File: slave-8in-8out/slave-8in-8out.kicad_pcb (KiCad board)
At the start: 2 copper layers, 61 x 72.4 mm, 87 parts, among them J1 Conn_01x06_Male, J2 Screw_Terminal_01x02, J3 Conn_01x06_Female, J4 Screw_Terminal_01x04, J5 Screw_Terminal_01x04, J6 Screw_Terminal_01x04, J7 Screw_Terminal_01x04, J8 Conn_01x10_Male, J9 Screw_Terminal_01x02, SW1 SW_DIP_x05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

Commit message: update slave-8in-8out pcb
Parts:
- moved R1 7.47 mm to (70.6, 96.5), turned to 0 degrees
- moved R2 5.71 mm to (70.6, 97.8), turned to 0 degrees
- moved D3 1.27 mm to (105.9, 104.6)
- moved D7 1.27 mm to (93.2, 104.6)
- moved R47 1.27 mm to (111.3, 106.9)
- moved R53 1.27 mm to (95.8, 106.9)
- moved R54 1.27 mm to (100.8, 106.9)
- moved D1 1.27 mm to (111.2, 104.6)
- moved D2 1.27 mm to (108.5, 104.6)
- moved D4 1.27 mm to (103.4, 104.6)
- moved D5 1.27 mm to (100.8, 104.6)
- moved D6 1.27 mm to (98.3, 104.6)
- moved D8 1.27 mm to (95.8, 104.6)
- moved J8 1.27 mm to (90.7, 111.3)
- moved R48 1.27 mm to (108.5, 106.9)
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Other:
- board text removed: "SCL"

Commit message: slave-8in-8out-0.1
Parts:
- removed R11: 10k, Resistor_SMD:R_0402_1005Metric
- U1: value MCP23017_SO -> PCF8575; footprint Package_SO:SOIC-28W_7.5x17.9mm_P1.27mm -> Package_SO:SSOP-24_5.3x8.2mm_P0.65mm
- moved H2 83.9 mm to (135.6, 63.8)
- moved H4 60.1 mm to (135.6, 128.3)
- moved H3 51.0 mm to (73.2, 128.3)
- moved J3 14.9 mm to (128.2, 101.3)
- moved U10 14.1 mm to (115.3, 96.7)
- moved U1 12.0 mm to (95.0, 96.7), turned to 0 degrees
- moved D1 11.6 mm to (122.2, 108.7)
- moved D3 11.6 mm to (116.8, 108.7)
- moved D5 11.6 mm to (111.8, 108.7)
- moved D7 11.6 mm to (104.1, 108.7)
- moved D8 11.6 mm to (106.7, 108.7)
- moved J8 11.6 mm to (101.6, 115.3)
- moved R47 11.6 mm to (122.2, 111.0)
- moved R48 11.6 mm to (119.4, 111.0)
- moved R50 11.6 mm to (114.3, 111.0)
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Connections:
- D7 pad 2: GPB7 -> GPA1
- D8 pad 2: GPA1 -> GPA0
- R46 pad 1: GPA0 -> GPB7
- U1 pad 1: GPB0 -> unconnected-(U1-Pad1)
- U1 pad 10: GND -> GPB6
- U1 pad 11: unconnected-(U1-Pad11) -> GPB7
- U1 pad 12: SCL -> GND
- U1 pad 13: SDA -> GPA0
- U1 pad 14: unconnected-(U1-Pad14) -> GPA1
- U1 pad 15: A0 -> GPA2
- U1 pad 16: A1 -> GPA3
- U1 pad 17: A2 -> GPA4
- U1 pad 18: Net-(R11-Pad1) -> GPA5
- U1 pad 19: unconnected-(U1-Pad19) -> GPA6
- U1 pad 2: GPB1 -> A1
- U1 pad 20: unconnected-(U1-Pad20) -> GPA7
- U1 pad 21: GPA0 -> A0
- U1 pad 22: GPA1 -> SCL
- U1 pad 23: GPA2 -> SDA
- U1 pad 24: GPA3 -> +3V3
- U1 pad 3: GPB2 -> A2
- U1 pad 4: GPB3 -> GPB0
- U1 pad 5: GPB4 -> GPB1
- U1 pad 6: GPB5 -> GPB2
- U1 pad 7: GPB6 -> GPB3
- U1 pad 8: GPB7 -> GPB4
- U1 pad 9: +3V3 -> GPB5
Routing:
- net +5V: track 0.00 -> 179.3 mm
- net GNDPWR: track 0.00 -> 169.6 mm
- net LED_GNDPWR: track 0.00 -> 156.4 mm, vias 0 -> 4
- net GND: track 0.00 -> 136.3 mm, vias 0 -> 5
- net +3V3: track 0.00 -> 92.1 mm, vias 0 -> 3
- net SCL: track 0.00 -> 77.7 mm, vias 0 -> 2
- net SDA: track 0.00 -> 67.6 mm, vias 0 -> 7
- net GPA4: track 0.00 -> 50.0 mm
- net A2: track 0.00 -> 48.5 mm, vias 0 -> 2
- net LED_GND: track 0.00 -> 47.8 mm
- net GPA6: track 0.00 -> 47.7 mm, vias 0 -> 3
- net A1: track 0.00 -> 46.8 mm, vias 0 -> 2
- net GPA7: track 0.00 -> 44.2 mm, vias 0 -> 3
- net GPB7: track 0.00 -> 43.1 mm, vias 0 -> 2
- net GPA5: track 0.00 -> 43.1 mm, vias 0 -> 3
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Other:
- board size 61 x 72.4 mm -> 69.6 x 71.6 mm
- board text added: "3.3V"
- board text added: "5V"
- board text added: "GNDPWR"
- board text added: "SCL"
- board text added: "SDA"
- board text added: "slave-8in-8out-0.1"
- board text removed: "1-2-3 Address"
- board text removed: "4-5 Led"
- board text removed: "brick slave 8in/8out v1.1"

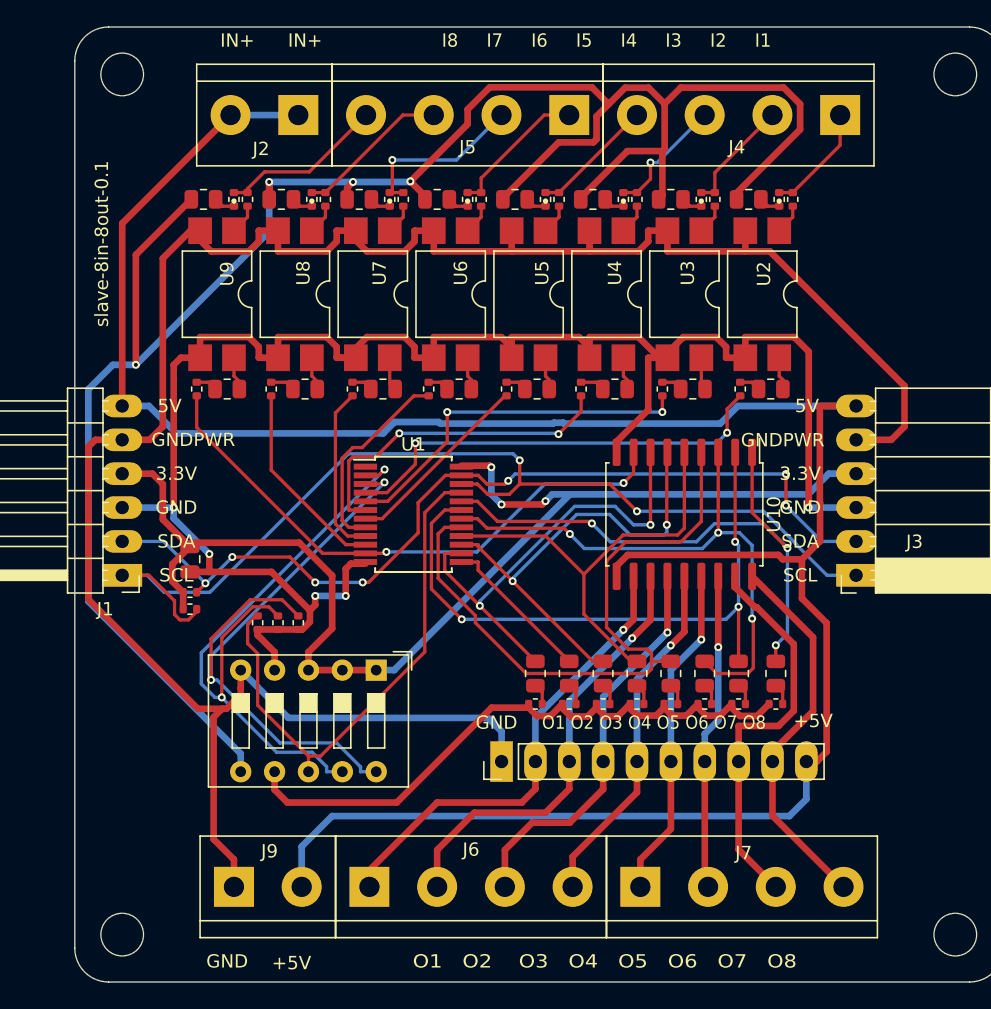
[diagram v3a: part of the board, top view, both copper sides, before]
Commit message: refactoring slave-8in-8out
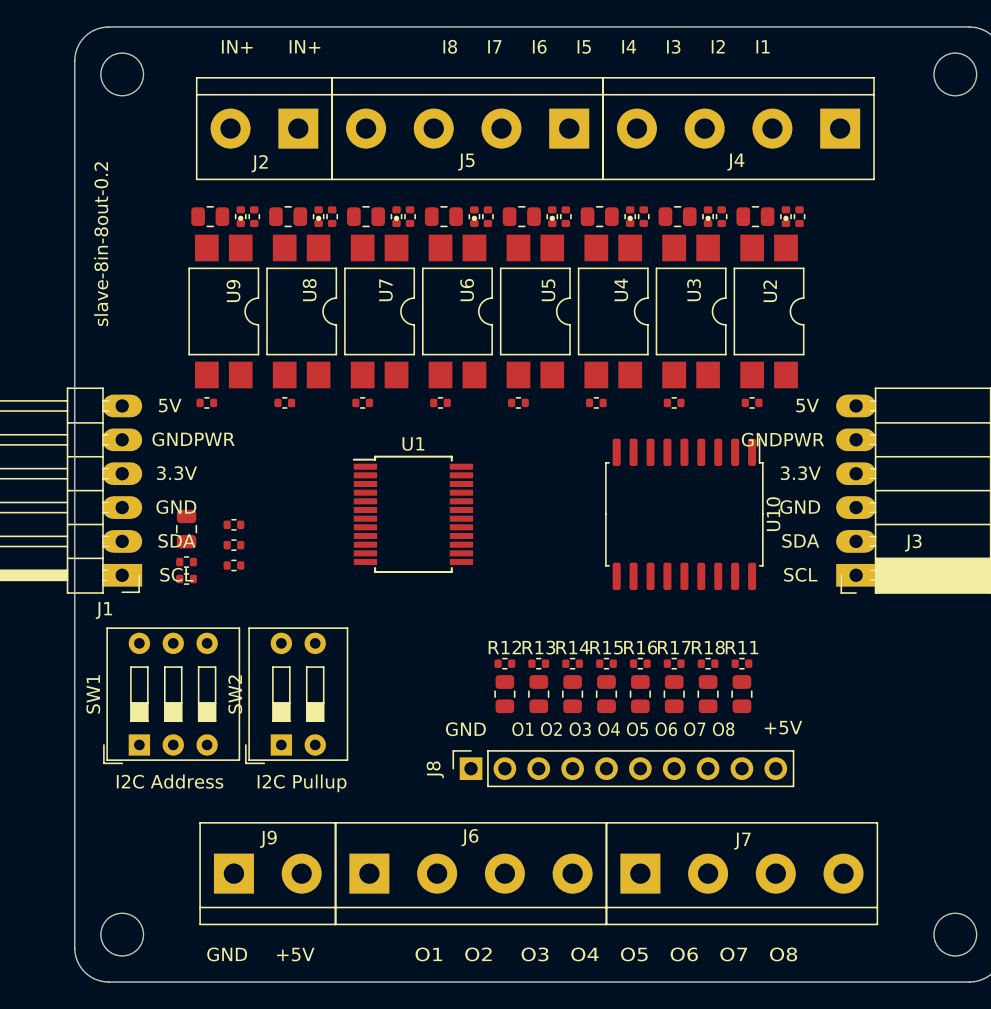
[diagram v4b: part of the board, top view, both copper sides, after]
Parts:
- removed D10, D12, D14, D16, D18, D20, D22, D24: LED, Resistor_SMD:R_0805_2012Metric
- removed R47, R48, R49, R50, R51, R52, R53, R54: 330, Resistor_SMD:R_0402_1005Metric
- added R11: 680, Resistor_SMD:R_0402_1005Metric, F.Cu at (119.6, 108.0)
- added R12: 680, Resistor_SMD:R_0402_1005Metric, F.Cu at (101.9, 108.0)
- added R13: 680, Resistor_SMD:R_0402_1005Metric, F.Cu at (104.4, 108.0)
- added R14: 680, Resistor_SMD:R_0402_1005Metric, F.Cu at (106.9, 108.0)
- added R15: 680, Resistor_SMD:R_0402_1005Metric, F.Cu at (109.5, 108.0)
- added R16: 680, Resistor_SMD:R_0402_1005Metric, F.Cu at (112.0, 108.0)
- added R17: 680, Resistor_SMD:R_0402_1005Metric, F.Cu at (114.6, 108.0)
- added R18: 680, Resistor_SMD:R_0402_1005Metric, F.Cu at (117.1, 108.0)
- added SW2: SW_DIP_x02, Button_Switch_THT:SW_DIP_SPSTx02_Slide_9.78x7.26mm_W7.62mm_P2.54mm, F.Cu at (85.1, 114.0)
- J8: value Conn_01x10_Male -> Conn_01x10_Female; footprint Connector_PinHeader_2.54mm:PinHeader_1x10_P2.54mm_Vertical -> Connector_PinSocket_2.54mm:PinSocket_1x10_P2.54mm_Vertical
- R31, R34, R37, R40, R43, R46, R5, R8: value 330 -> 10k
- SW1: value SW_DIP_x05 -> SW_DIP_x03; footprint Button_Switch_THT:SW_DIP_SPSTx05_Slide_9.78x14.88mm_W7.62mm_P2.54mm -> Button_Switch_THT:SW_DIP_SPSTx03_Slide_9.78x9.8mm_W7.62mm_P2.54mm
- moved D1 20.4 mm to (101.9, 110.2), turned to -90 degrees
- moved SW1 18.6 mm to (74.4, 114.0), turned to 90 degrees
- moved D2 15.1 mm to (104.4, 110.2), turned to -90 degrees
- moved D7 13.0 mm to (117.1, 110.2), turned to -90 degrees
- moved D8 13.0 mm to (119.6, 110.2), turned to -90 degrees
- moved D3 10.0 mm to (106.9, 110.2), turned to -90 degrees
- moved R28 8.79 mm to (81.5, 97.5), turned to 0 degrees
- moved R29 6.69 mm to (81.5, 99.1), turned to 0 degrees
- moved D6 5.55 mm to (114.6, 110.2), turned to -90 degrees
- moved D4 5.07 mm to (109.5, 110.2), turned to -90 degrees
- moved R30 4.65 mm to (81.5, 100.6), turned to 0 degrees
- moved J8 2.35 mm to (99.3, 115.8)
- moved C1 2.28 mm to (78.0, 97.9)
- moved R2 2.28 mm to (78.0, 101.6)
- moved R1 2.28 mm to (78.0, 100.3)
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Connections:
- C1 pad 2: GND -> LED_GND
- D1 pad 2: GPA7 -> O1
- D11 pad 1: LED_GNDPWR -> GNDPWR
- D13 pad 1: LED_GNDPWR -> GNDPWR
- D15 pad 1: LED_GNDPWR -> GNDPWR
- D17 pad 1: LED_GNDPWR -> GNDPWR
- D19 pad 1: LED_GNDPWR -> GNDPWR
- D2 pad 2: GPA6 -> O2
- D21 pad 1: LED_GNDPWR -> GNDPWR
- D23 pad 1: LED_GNDPWR -> GNDPWR
- D3 pad 2: GPA5 -> O3
- D4 pad 2: GPA4 -> O4
- D5 pad 2: GPA3 -> O5
- D6 pad 2: GPA2 -> O6
- D7 pad 2: GPA1 -> O7
- D8 pad 2: GPA0 -> O8
- D9 pad 1: LED_GNDPWR -> GNDPWR
- J1 pad 3: GND -> LED_GND
- J3 pad 3: GND -> LED_GND
- R1 pad 1: +3V3 -> Net-(R1-Pad1)
- R2 pad 1: +3V3 -> Net-(R2-Pad1)
- R28 pad 2: GND -> LED_GND
- R29 pad 2: GND -> LED_GND
- R30 pad 2: GND -> LED_GND
- R31 pad 1: GPB2 -> LED_GND
- R31 pad 2: Net-(D14-Pad2) -> GPB2
- R34 pad 1: GPB3 -> LED_GND
- R34 pad 2: Net-(D16-Pad2) -> GPB3
- R37 pad 1: GPB4 -> LED_GND
- R37 pad 2: Net-(D18-Pad2) -> GPB4
- R40 pad 1: GPB5 -> LED_GND
- R40 pad 2: Net-(D20-Pad2) -> GPB5
- R43 pad 1: GPB6 -> LED_GND
- R43 pad 2: Net-(D22-Pad2) -> GPB6
- R46 pad 1: GPB7 -> LED_GND
- R46 pad 2: Net-(D24-Pad2) -> GPB7
- R5 pad 1: GPB0 -> LED_GND
- R5 pad 2: Net-(D10-Pad2) -> GPB0
- R8 pad 1: GPB1 -> LED_GND
- R8 pad 2: Net-(D12-Pad2) -> GPB1
- SW1 pad 4: GND -> A0
- SW1 pad 5: GNDPWR -> A1
- SW1 pad 6: LED_GNDPWR -> A2
- U1 pad 12: GND -> LED_GND
- U10 pad 8: GPB7 -> GPA0
- U10 pad 9: GND -> LED_GND
- U2 pad 3: GND -> GPB0
- U2 pad 4: Net-(D10-Pad1) -> +3V3
- U3 pad 3: GND -> GPB1
- U3 pad 4: Net-(D12-Pad1) -> +3V3
- U4 pad 3: GND -> GPB2
- U4 pad 4: Net-(D14-Pad1) -> +3V3
- U5 pad 3: GND -> GPB3
- U5 pad 4: Net-(D16-Pad1) -> +3V3
- U6 pad 3: GND -> GPB4
- U6 pad 4: Net-(D18-Pad1) -> +3V3
- U7 pad 3: GND -> GPB5
- U7 pad 4: Net-(D20-Pad1) -> +3V3
- U8 pad 3: GND -> GPB6
- U8 pad 4: Net-(D22-Pad1) -> +3V3
- U9 pad 3: GND -> GPB7
- U9 pad 4: Net-(D24-Pad1) -> +3V3
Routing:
- net +5V: track 179.3 -> 0.00 mm
- net GNDPWR: track 169.6 -> 0.00 mm
- net LED_GNDPWR: track 156.4 -> 0.00 mm, vias 4 -> 0
- net GND: track 136.3 -> 0.00 mm, vias 5 -> 0
- net +3V3: track 92.1 -> 0.00 mm, vias 3 -> 0
- net SCL: track 77.7 -> 0.00 mm, vias 2 -> 0
- net SDA: track 67.6 -> 0.00 mm, vias 7 -> 0
- net GPA4: track 50.0 -> 0.00 mm
- net A2: track 48.5 -> 0.00 mm, vias 2 -> 0
- net LED_GND: track 47.8 -> 0.00 mm
- net GPA6: track 47.7 -> 0.00 mm, vias 3 -> 0
- net A1: track 46.8 -> 0.00 mm, vias 2 -> 0
- net GPA7: track 44.2 -> 0.00 mm, vias 3 -> 0
- net GPB7: track 43.1 -> 0.00 mm, vias 2 -> 0
- net GPA5: track 43.1 -> 0.00 mm, vias 3 -> 0
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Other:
- board text added: "I2C Address"
- board text added: "I2C Pullup"
- board text added: "slave-8in-8out-0.2"
- board text removed: "slave-8in-8out-0.1"

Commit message: update slave-8in-8out
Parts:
- added R19: 10k, Resistor_SMD:R_0402_1005Metric, F.Cu at (96.8, 93.0)
- added R20: 10k, Resistor_SMD:R_0402_1005Metric, F.Cu at (96.8, 94.5)
- added R21: 10k, Resistor_SMD:R_0402_1005Metric, F.Cu at (96.8, 97.5)
- added R22: 10k, Resistor_SMD:R_0402_1005Metric, F.Cu at (96.8, 96.0)
- added R23: 10k, Resistor_SMD:R_0402_1005Metric, F.Cu at (96.8, 99.1)
- added R24: 10k, Resistor_SMD:R_0402_1005Metric, F.Cu at (96.8, 100.6)
- added R25: 10k, Resistor_SMD:R_0402_1005Metric, F.Cu at (96.8, 102.1)
- added R26: 10k, Resistor_SMD:R_0402_1005Metric, F.Cu at (96.8, 103.6)
- moved U1 4.51 mm to (90.7, 98.0)
- moved D1 1.54 mm to (100.3, 110.5), turned to 90 degrees
- moved D2 1.54 mm to (102.9, 110.5), turned to 90 degrees
- moved D3 1.54 mm to (105.4, 110.5), turned to 90 degrees
- moved D4 1.54 mm to (108.0, 110.5), turned to 90 degrees
- moved D5 1.54 mm to (110.5, 110.5), turned to 90 degrees
- moved D6 1.54 mm to (113.0, 110.5), turned to 90 degrees
- moved D7 1.54 mm to (115.6, 110.5), turned to 90 degrees
- moved D8 1.54 mm to (118.1, 110.5), turned to 90 degrees
- moved R11 1.54 mm to (118.1, 108.2)
- moved R12 1.54 mm to (100.3, 108.2)
- moved R13 1.54 mm to (102.9, 108.2)
- moved R14 1.54 mm to (105.4, 108.2)
- moved R15 1.54 mm to (108.0, 108.2)
- moved R16 1.54 mm to (110.5, 108.2)
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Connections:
- C1 pad 2: LED_GND -> GND
- D1 pad 1: Net-(D1-Pad1) -> O0
- D1 pad 2: O1 -> Net-(R12-Pad1)
- D2 pad 1: Net-(D2-Pad1) -> O1
- D2 pad 2: O2 -> Net-(R13-Pad1)
- D3 pad 1: Net-(D3-Pad1) -> O2
- D3 pad 2: O3 -> Net-(R14-Pad1)
- D4 pad 1: Net-(D4-Pad1) -> O3
- D4 pad 2: O4 -> Net-(D4-Pad2)
- D5 pad 1: Net-(D5-Pad1) -> O4
- D5 pad 2: O5 -> Net-(D5-Pad2)
- D6 pad 1: Net-(D6-Pad1) -> O5
- D6 pad 2: O6 -> Net-(D6-Pad2)
- D7 pad 1: Net-(D7-Pad1) -> O6
- D7 pad 2: O7 -> Net-(D7-Pad2)
- D8 pad 1: Net-(D8-Pad1) -> O7
- D8 pad 2: O8 -> Net-(D8-Pad2)
- J1 pad 3: LED_GND -> GND
- J3 pad 3: LED_GND -> GND
- J4 pad 1: I1 -> I0
- J4 pad 2: I2 -> I1
- J4 pad 3: I3 -> I2
- J4 pad 4: I4 -> I3
- J5 pad 1: I5 -> I4
- J5 pad 2: I6 -> I5
- J5 pad 3: I7 -> I6
- J5 pad 4: I8 -> I7
- J6 pad 1: O1 -> O0
- J6 pad 2: O2 -> O1
- J6 pad 3: O3 -> O2
- J6 pad 4: O4 -> O3
- J7 pad 1: O5 -> O4
- J7 pad 2: O6 -> O5
- J7 pad 3: O7 -> O6
- J7 pad 4: O8 -> O7
- J8 pad 2: O1 -> O0
- J8 pad 3: O2 -> O1
- J8 pad 4: O3 -> O2
- J8 pad 5: O4 -> O3
- J8 pad 6: O5 -> O4
- J8 pad 7: O6 -> O5
- J8 pad 8: O7 -> O6
- J8 pad 9: O8 -> O7
- R10 pad 2: I3 -> I2
- R11 pad 1: Net-(D8-Pad1) -> Net-(D8-Pad2)
- R11 pad 2: LED_GND -> +5V
- R12 pad 1: Net-(D1-Pad1) -> Net-(R12-Pad1)
- R12 pad 2: LED_GND -> +5V
- R13 pad 1: Net-(D2-Pad1) -> Net-(R13-Pad1)
- R13 pad 2: LED_GND -> +5V
- R14 pad 1: Net-(D3-Pad1) -> Net-(R14-Pad1)
- R14 pad 2: LED_GND -> +5V
- R15 pad 1: Net-(D4-Pad1) -> Net-(D4-Pad2)
- R15 pad 2: LED_GND -> +5V
- R16 pad 1: Net-(D5-Pad1) -> Net-(D5-Pad2)
- R16 pad 2: LED_GND -> +5V
- R17 pad 1: Net-(D6-Pad1) -> Net-(D6-Pad2)
- R17 pad 2: LED_GND -> +5V
- R18 pad 1: Net-(D7-Pad1) -> Net-(D7-Pad2)
- R18 pad 2: LED_GND -> +5V
- R28 pad 2: LED_GND -> GND
- R29 pad 2: LED_GND -> GND
- R3 pad 1: I1 -> I0
- R30 pad 2: LED_GND -> GND
- R31 pad 1: LED_GND -> GND
- R32 pad 1: I4 -> I3
- R33 pad 2: I4 -> I3
- R34 pad 1: LED_GND -> GND
- R35 pad 1: I5 -> I4
- R36 pad 2: I5 -> I4
- R37 pad 1: LED_GND -> GND
- R38 pad 1: I6 -> I5
- R39 pad 2: I6 -> I5
- R4 pad 2: I1 -> I0
- R40 pad 1: LED_GND -> GND
- R41 pad 1: I7 -> I6
- R42 pad 2: I7 -> I6
- R43 pad 1: LED_GND -> GND
- R44 pad 1: I8 -> I7
- R45 pad 2: I8 -> I7
- R46 pad 1: LED_GND -> GND
- R5 pad 1: LED_GND -> GND
- R6 pad 1: I2 -> I1
- R7 pad 2: I2 -> I1
- R8 pad 1: LED_GND -> GND
- R9 pad 1: I3 -> I2
- U1 pad 12: LED_GND -> GND
- U10 pad 11: O1 -> O0
- U10 pad 12: O2 -> O1
- U10 pad 13: O3 -> O2
- U10 pad 14: O4 -> O3
- U10 pad 15: O5 -> O4
- U10 pad 16: O6 -> O5
- U10 pad 17: O7 -> O6
- U10 pad 18: O8 -> O7
- U10 pad 9: LED_GND -> GND
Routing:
- net GNDPWR: track 0.00 -> 76.4 mm
- net +3V3: track 0.00 -> 69.1 mm, vias 0 -> 8
- net GND: track 0.00 -> 40.8 mm, vias 0 -> 8
- net +5V: track 0.00 -> 32.6 mm
- net O7: track 0.00 -> 4.68 mm
- net O6: track 0.00 -> 4.68 mm
- net O5: track 0.00 -> 4.68 mm
- net O4: track 0.00 -> 4.68 mm
- net O3: track 0.00 -> 4.68 mm
- net O2: track 0.00 -> 4.68 mm
- net O1: track 0.00 -> 4.68 mm
- net O0: track 0.00 -> 4.68 mm
- net GPB6: track 0.00 -> 3.08 mm
- net GPB5: track 0.00 -> 3.08 mm
- net GPB4: track 0.00 -> 3.08 mm
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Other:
- board text added: "I7 I6 I5 I4 I3 I2 I1 I0"
- board text added: "O0 O1 O2 O3 O4 O5 O6 O7"
- board text removed: "I8 I7 I6 I5 I4 I3 I2 I1"
- board text removed: "O1 O2 O3 O4 O5 O6 O7 O8"

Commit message: update slave-8in-8out pcb
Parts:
- U2, U3, U4, U5, U6, U7, U8, U9: value EL817 -> EL817S1(C)(TU)-F
- moved R31 1.67 mm to (109.0, 89.4)
- moved R34 1.67 mm to (103.2, 89.4)
- moved R37 1.67 mm to (97.3, 89.4)
- moved R43 1.67 mm to (85.6, 89.4)
- moved R46 1.67 mm to (79.8, 89.4)
- moved R5 1.67 mm to (120.6, 89.4)
- moved R8 1.67 mm to (114.8, 89.4)
- moved R40 1.67 mm to (91.5, 89.4)
- moved U2 1.17 mm to (120.8, 82.0)
- moved U3 1.17 mm to (115.0, 82.0)
- moved U4 1.17 mm to (109.1, 82.0)
- moved U5 1.17 mm to (103.3, 82.0)
- moved U6 1.17 mm to (97.4, 82.0)
- moved U7 1.17 mm to (91.6, 82.0)
- moved U8 1.17 mm to (85.8, 82.0)
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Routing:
- net GNDPWR: track 76.4 -> 88.1 mm
- net +3V3: track 69.1 -> 72.4 mm
- net GPB7: track 3.08 -> 4.42 mm
- net GPB1: track 2.36 -> 3.70 mm
- net GPB6: track 3.08 -> 4.42 mm
- net GPB5: track 3.08 -> 4.42 mm
- net GPB4: track 3.08 -> 4.42 mm
- net GPB3: track 3.08 -> 4.42 mm
- net GPB2: track 3.08 -> 4.42 mm
- net GPB0: track 3.02 -> 4.19 mm
- net I6: track 0.00 -> 1.02 mm
- net I3: track 0.00 -> 1.02 mm
- net I2: track 0.00 -> 1.02 mm
- net I1: track 0.00 -> 1.02 mm
- net I0: track 0.00 -> 1.02 mm
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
